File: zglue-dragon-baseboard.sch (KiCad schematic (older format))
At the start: 42 parts, among them U1 zGlue-Dragon

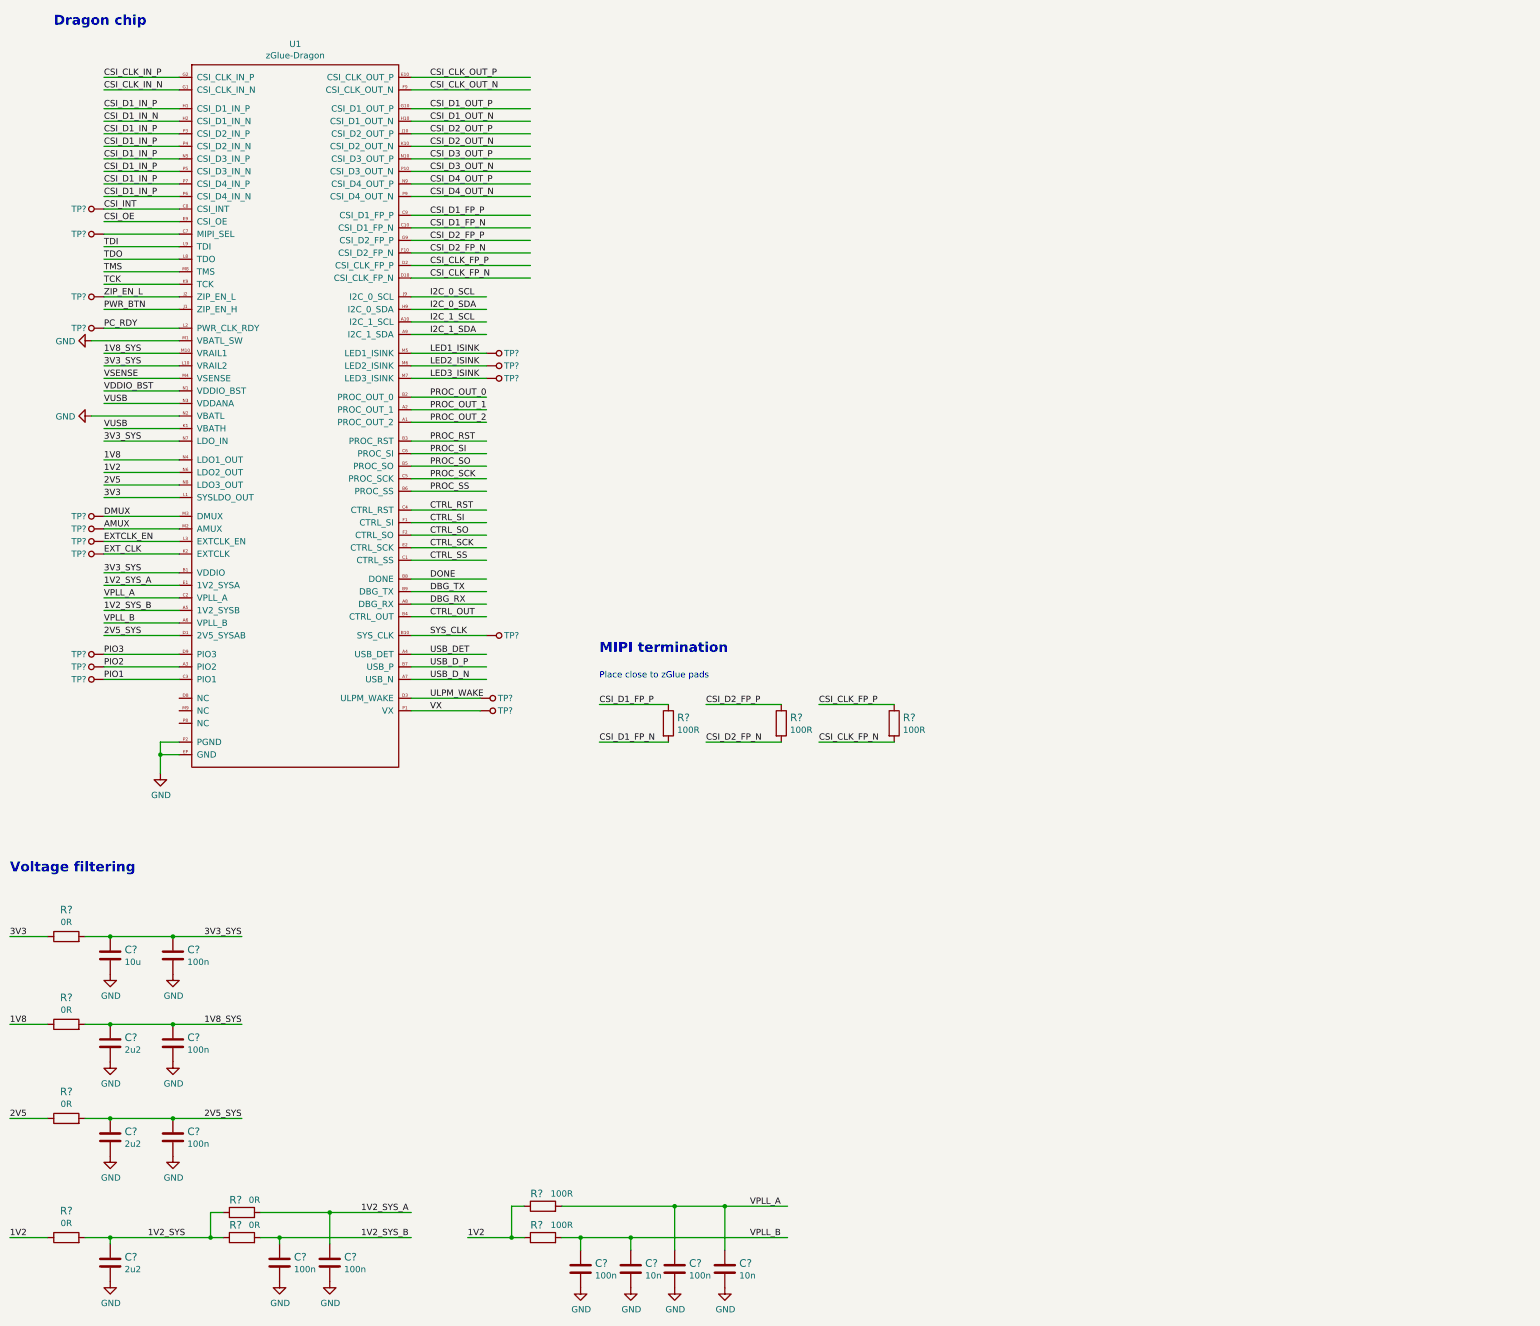
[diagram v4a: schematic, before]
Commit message: Added b2b connectors
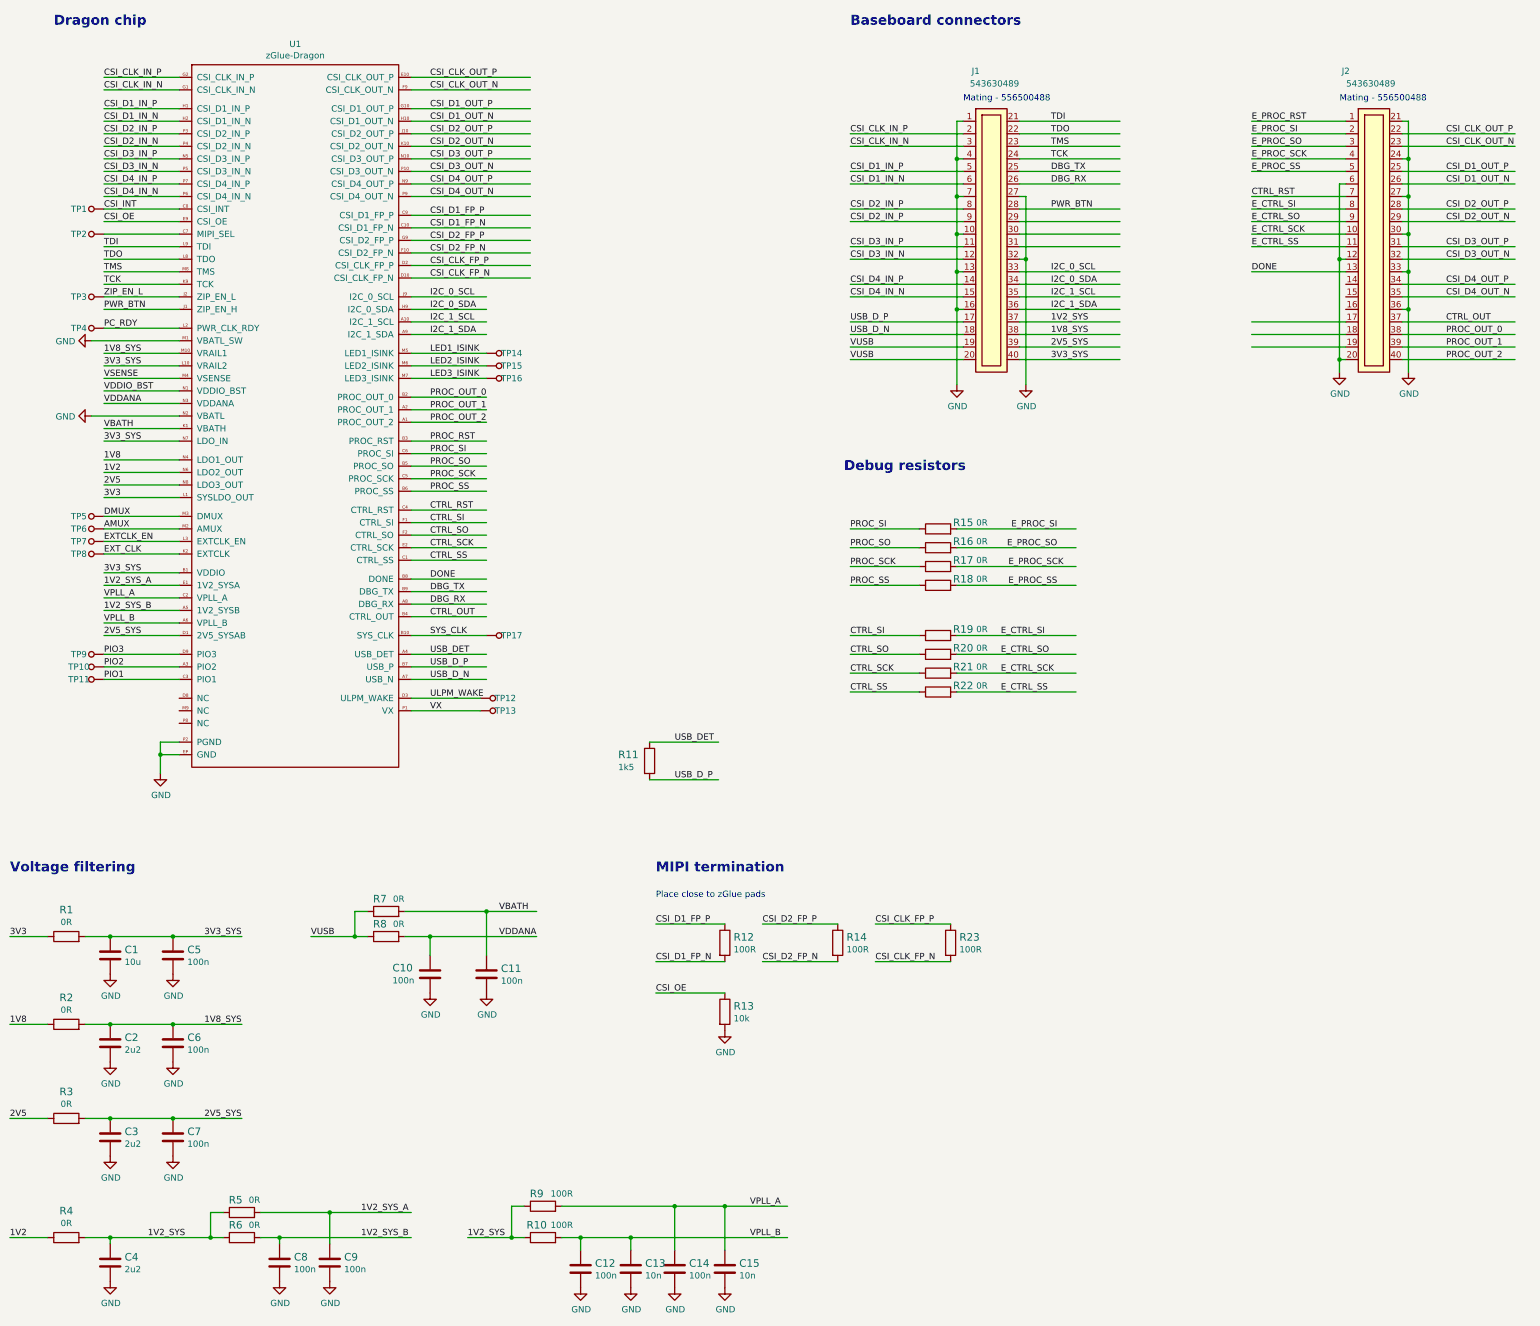
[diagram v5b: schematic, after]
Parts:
- added C10, C11: C_100n_0402_6V3, antmicro-footprints:0402-cap, symbol antmicroCapacitors0402:C_100n_0402_6V3
- added J1, J2: 543630489, antmicro-footprints:543630489, symbol antmicroB2bConnectors:543630489
- added R11: R_1k5_0402, antmicro-footprints:0402-res, symbol antmicroResistors0402:R_1k5_0402
- added R13: R_10k_0402, antmicro-footprints:0402-res, symbol antmicroResistors0402:R_10k_0402
- added R15, R16, R17, R18, R19, R20, R21, R22, R7, R8: R_0R_0402, antmicro-footprints:0402-res, symbol antmicroResistors0402:R_0R_0402
- gave numbers to parts that had none: 41
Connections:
- net labels added: CSI_D2_IN_N, CSI_D2_IN_P, CSI_D3_IN_N, CSI_D3_IN_P, CSI_D4_IN_N, CSI_D4_IN_P, E_CTRL_SCK, E_CTRL_SI, E_CTRL_SO, E_CTRL_SS, E_PROC_RST, E_PROC_SCK, E_PROC_SI, E_PROC_SO, E_PROC_SS, VBATH, VDDANA
- wire segments 141 -> 264
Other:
- note added: "Baseboard connectors"
- note added: "Debug resistors"
- note added: "Mating - 556500488"
- moved on the sheet: R12, R14, R23
